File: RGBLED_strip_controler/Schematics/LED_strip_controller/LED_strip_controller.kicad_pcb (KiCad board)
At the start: 2 copper layers, 21 parts, among them J1 LEDStrip, J2 LEDString, J3 Fountain, J4 Conn_01x03_Male, Q1 TIP120, SW1 SW_MEC_5G, SW2 SW_MEC_5G, U1 ATmega328P-PU, U2 L7805, X1 16MHz

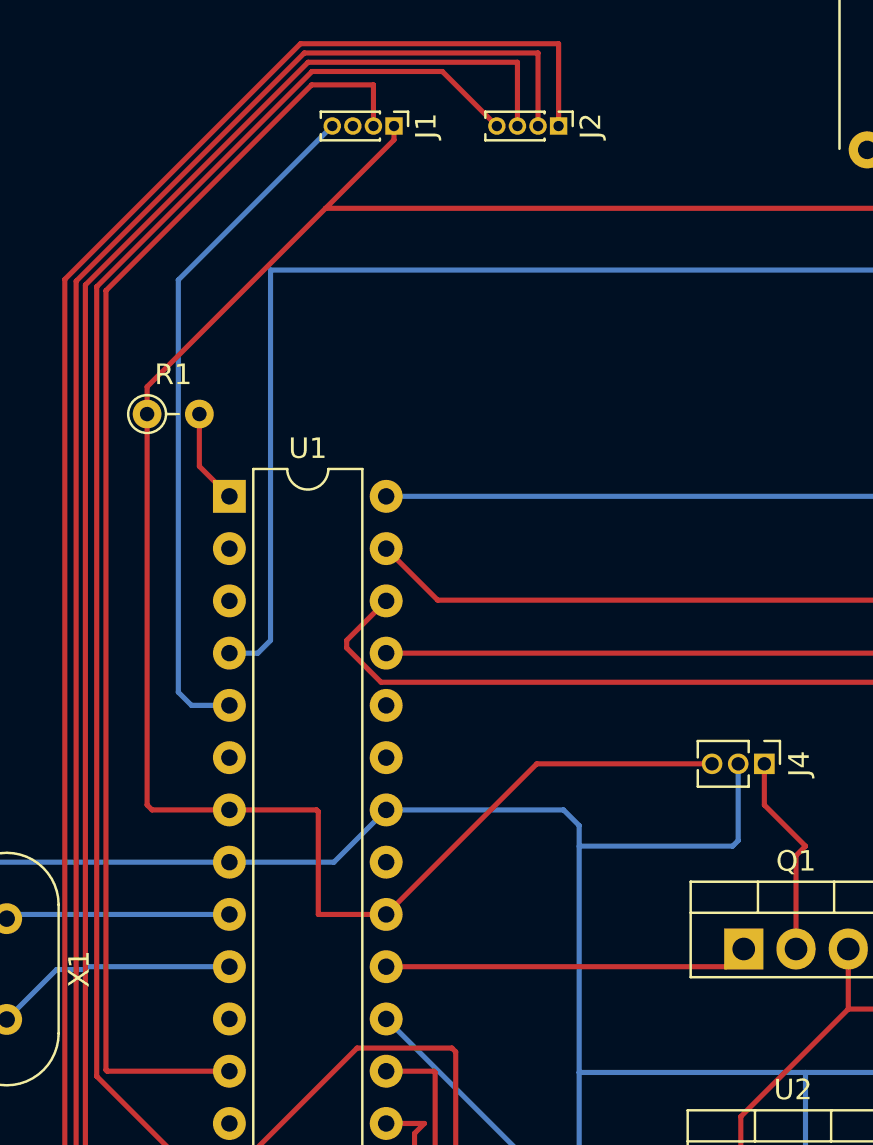
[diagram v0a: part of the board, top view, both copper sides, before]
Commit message: Schematic update
Corrected an error I made.
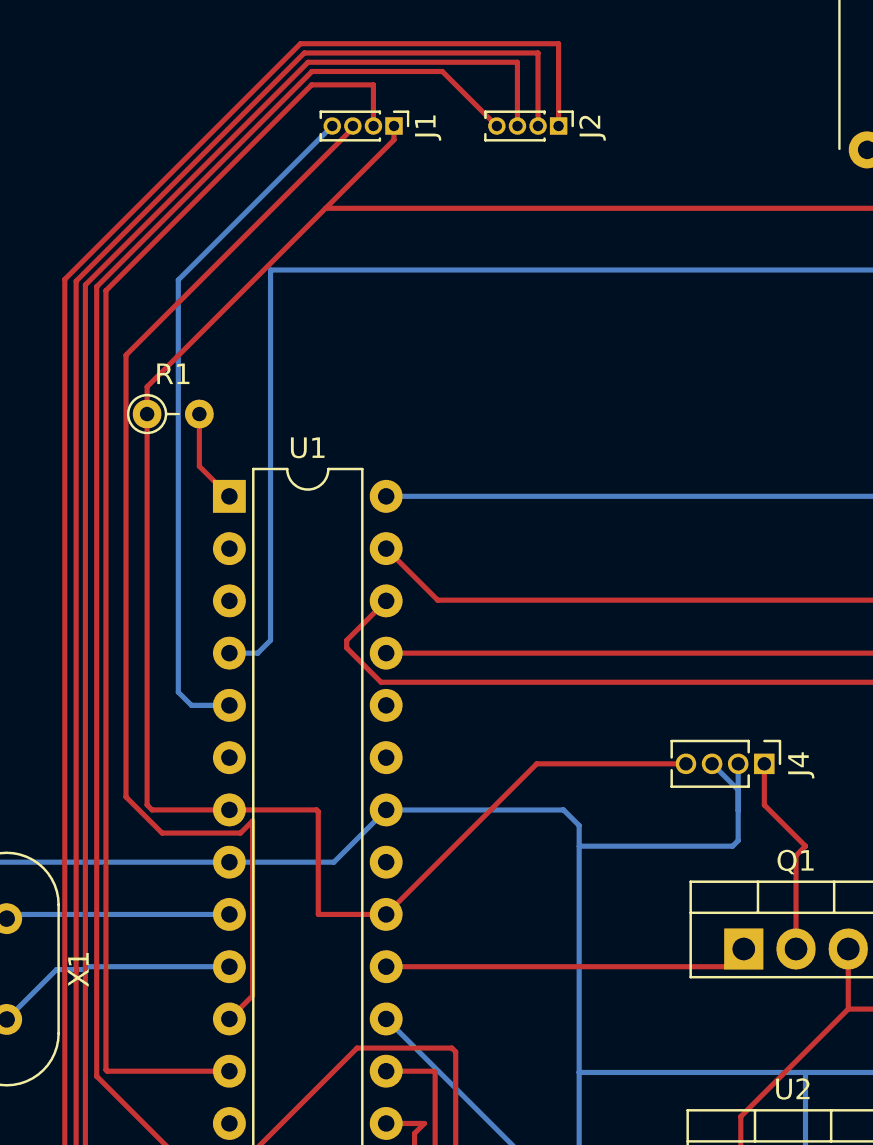
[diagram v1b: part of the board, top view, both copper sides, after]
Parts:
- J4: footprint Connector_PinHeader_1.27mm:PinHeader_1x03_P1.27mm_Vertical -> Connector_PinHeader_1.27mm:PinHeader_1x04_P1.27mm_Vertical
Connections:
- J1 pad 3: Net-(J1-Pad2) -> Net-(J1-Pad3)
- J4 pad 3: +5V -> GND
- U1 pad 11: Net-(J1-Pad2) -> Net-(J1-Pad3)
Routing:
- net Net-(J1-Pad3): track 0.00 -> 54.4 mm
- net GND: track 202.9 -> 205.7 mm
- net +5V: track 180.7 -> 179.4 mm
